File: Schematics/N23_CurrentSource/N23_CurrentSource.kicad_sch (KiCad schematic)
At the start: 64 parts

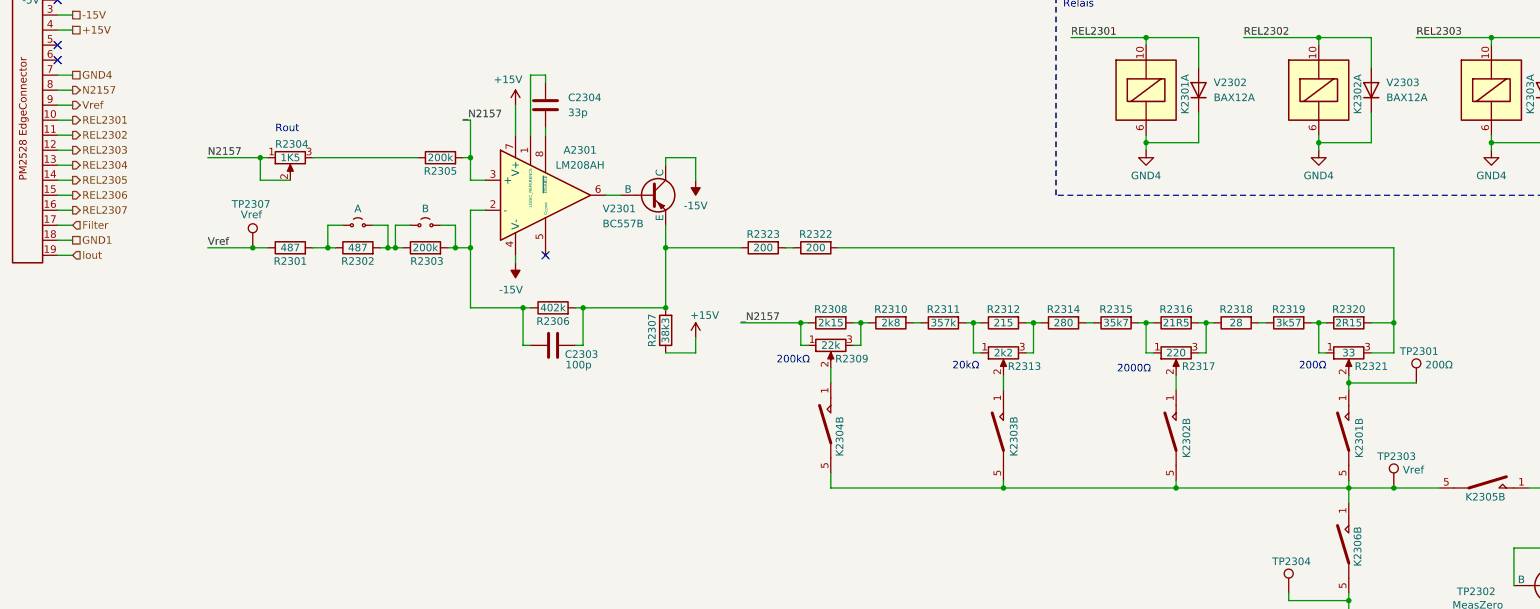
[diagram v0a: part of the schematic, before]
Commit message: Restructure folders, added EPROMs and Ghidra-project
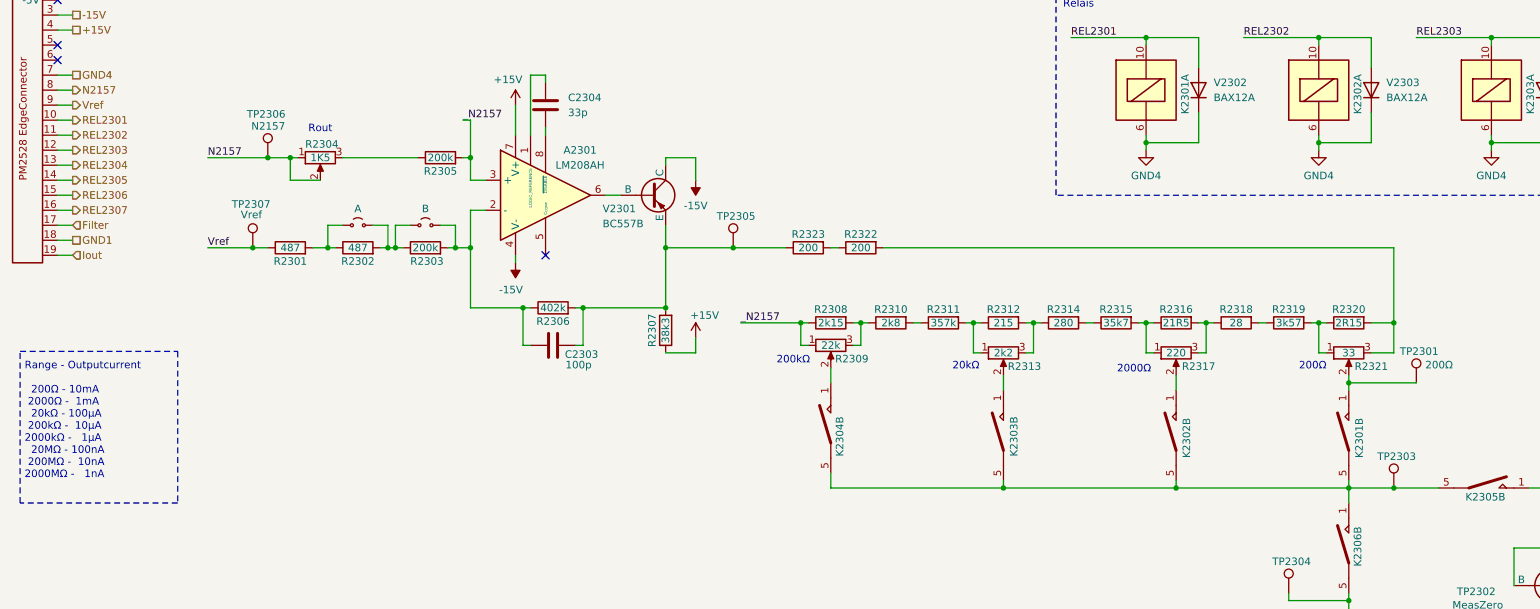
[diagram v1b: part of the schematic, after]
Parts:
- added TP2305: ~, Connector_PinHeader_1.00mm:PinHeader_1x01_P1.00mm_Vertical, symbol Connector:TestPoint
- added TP2306: N2157, Connector_PinHeader_1.00mm:PinHeader_1x01_P1.00mm_Vertical, symbol Connector:TestPoint
- C2301, C2302: footprint Capacitor_THT:C_Rect_L26.5mm_W8.5mm_P22.50mm_MKS4 -> Capacitor_THT:CP_Radial_Tantal_D4.5mm_P5.00mm
- C2303, C2304: footprint Capacitor_THT:C_Rect_L26.5mm_W8.5mm_P22.50mm_MKS4 -> Capacitor_THT:C_Disc_D4.3mm_W1.9mm_P5.00mm
- C2305: footprint Capacitor_THT:C_Rect_L26.5mm_W8.5mm_P22.50mm_MKS4 -> Capacitor_THT:C_Axial_L5.1mm_D3.1mm_P15.00mm_Horizontal
- R2303, R2305, R2306, R2311, R2322, R2323, R2332, R2333: footprint Resistor_THT:R_Axial_DIN0207_L6.3mm_D2.5mm_P10.16mm_Horizontal -> Resistor_THT:R_Axial_DIN0309_L9.0mm_D3.2mm_P12.70mm_Horizontal
- R2324: footprint Resistor_THT:R_Axial_DIN0207_L6.3mm_D2.5mm_P10.16mm_Horizontal -> Resistor_THT:R_Axial_DIN0614_L14.3mm_D5.7mm_P25.40mm_Horizontal
- R2325: footprint Resistor_THT:R_Axial_DIN0207_L6.3mm_D2.5mm_P10.16mm_Horizontal -> Varistor:RV_Disc_D7mm_W3.9mm_P5mm
- R2330: footprint Resistor_THT:R_Axial_DIN0207_L6.3mm_D2.5mm_P10.16mm_Horizontal -> Resistor_THT:R_Axial_DIN0411_L9.9mm_D3.6mm_P15.24mm_Horizontal
- TP2303: value Vref -> ~
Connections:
- net N2157: now also TP2306.1
- net at C2303.1, R2306.2, R2307.2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: now also TP2305.1
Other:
- note added: "Range - Outputcurrent 200Ω - 10mA 2000Ω - 1mA 20kΩ - 100µA 200kΩ - 10µA 2000kΩ - 1µA 20MΩ - 100nA 200MΩ - 10nA 2000MΩ - 1nA"
- moved on the sheet: R2304, R2322, R2323

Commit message: Lotsofchanges. Included Ghidra-project and correct firmware-images
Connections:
- net at R2320.2, R2322.2: now also R2321.1; no longer R2321.3
- net at R2319.2, R2320.1: now also R2321.3; no longer R2321.1
- net at R2311.2, R2312.1: now also R2313.3; no longer R2313.1
- net at R2312.2, R2314.1: now also R2313.1; no longer R2313.3
- net at R2308.2, R2310.1: now also R2309.1; no longer R2309.3
- net at R2316.2, R2318.1: now also R2317.1; no longer R2317.3
- net at R2315.2, R2316.1: now also R2317.3; no longer R2317.1
- net _N2157: no longer names the net of A2301.3 (+), R2305.2, R2308.1
- net _N2157: now also R2309.3; no longer R2309.1
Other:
- moved on the sheet: A2301, C2303, C2304, C2305, K2301B, K2302B, K2303B, K2305B, K2306B, K2307B, R2301, R2302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
